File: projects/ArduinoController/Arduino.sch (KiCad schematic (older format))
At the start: 56 parts

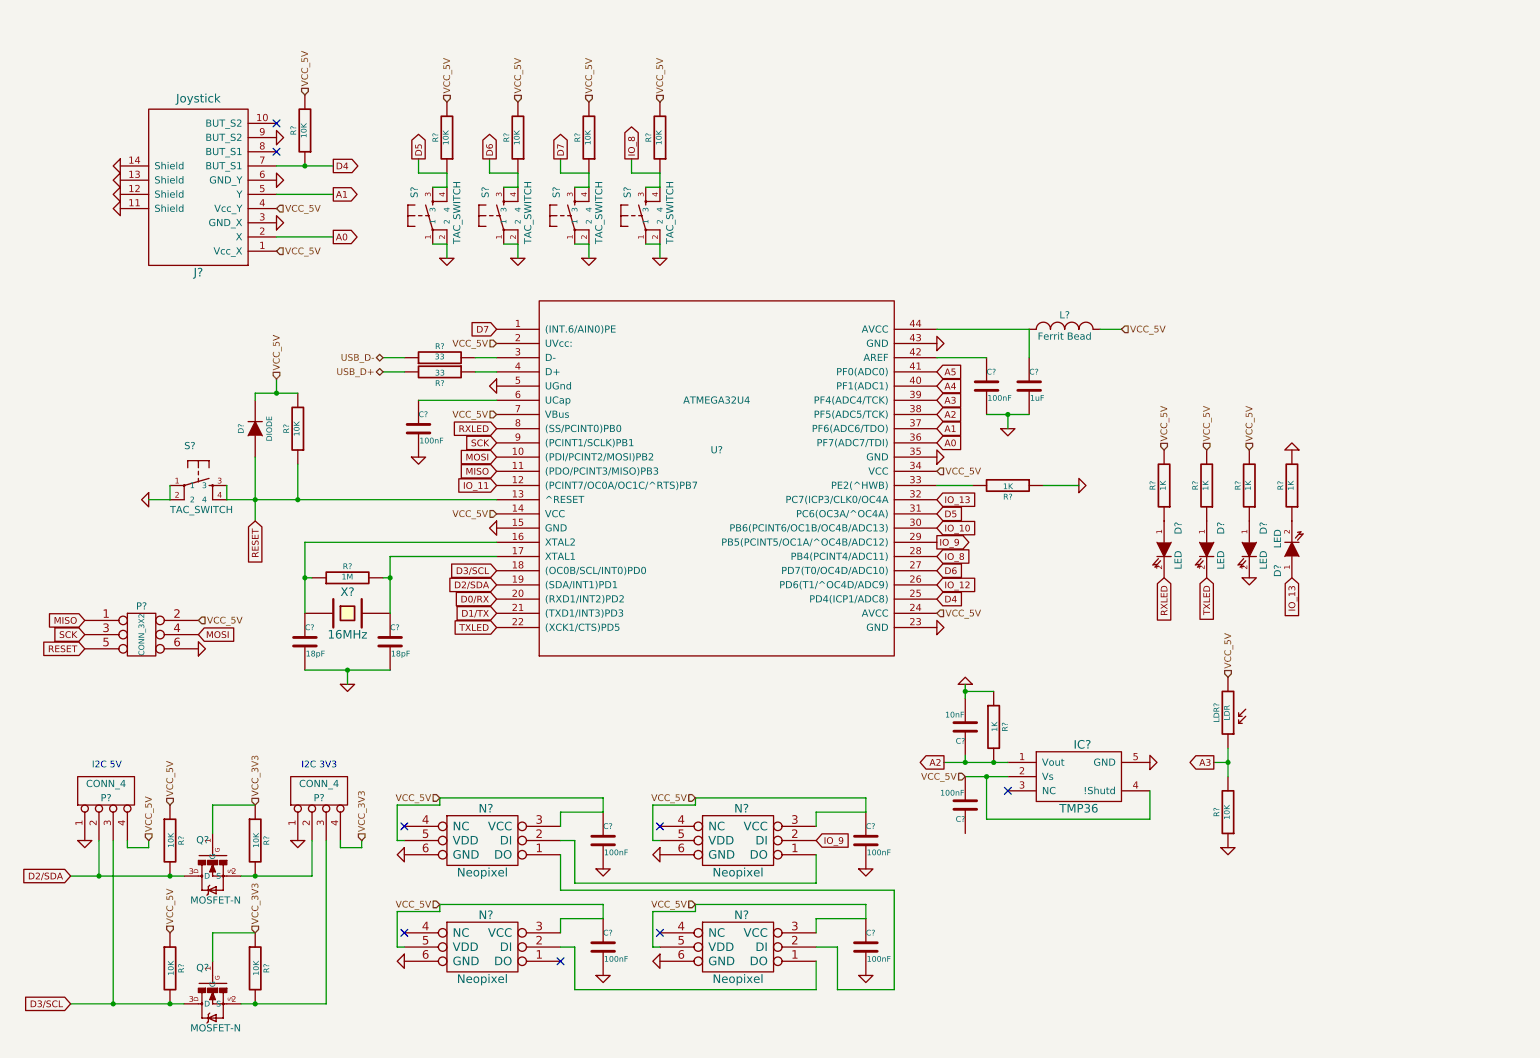
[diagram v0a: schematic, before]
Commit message: working on schematics of Arduino Controller
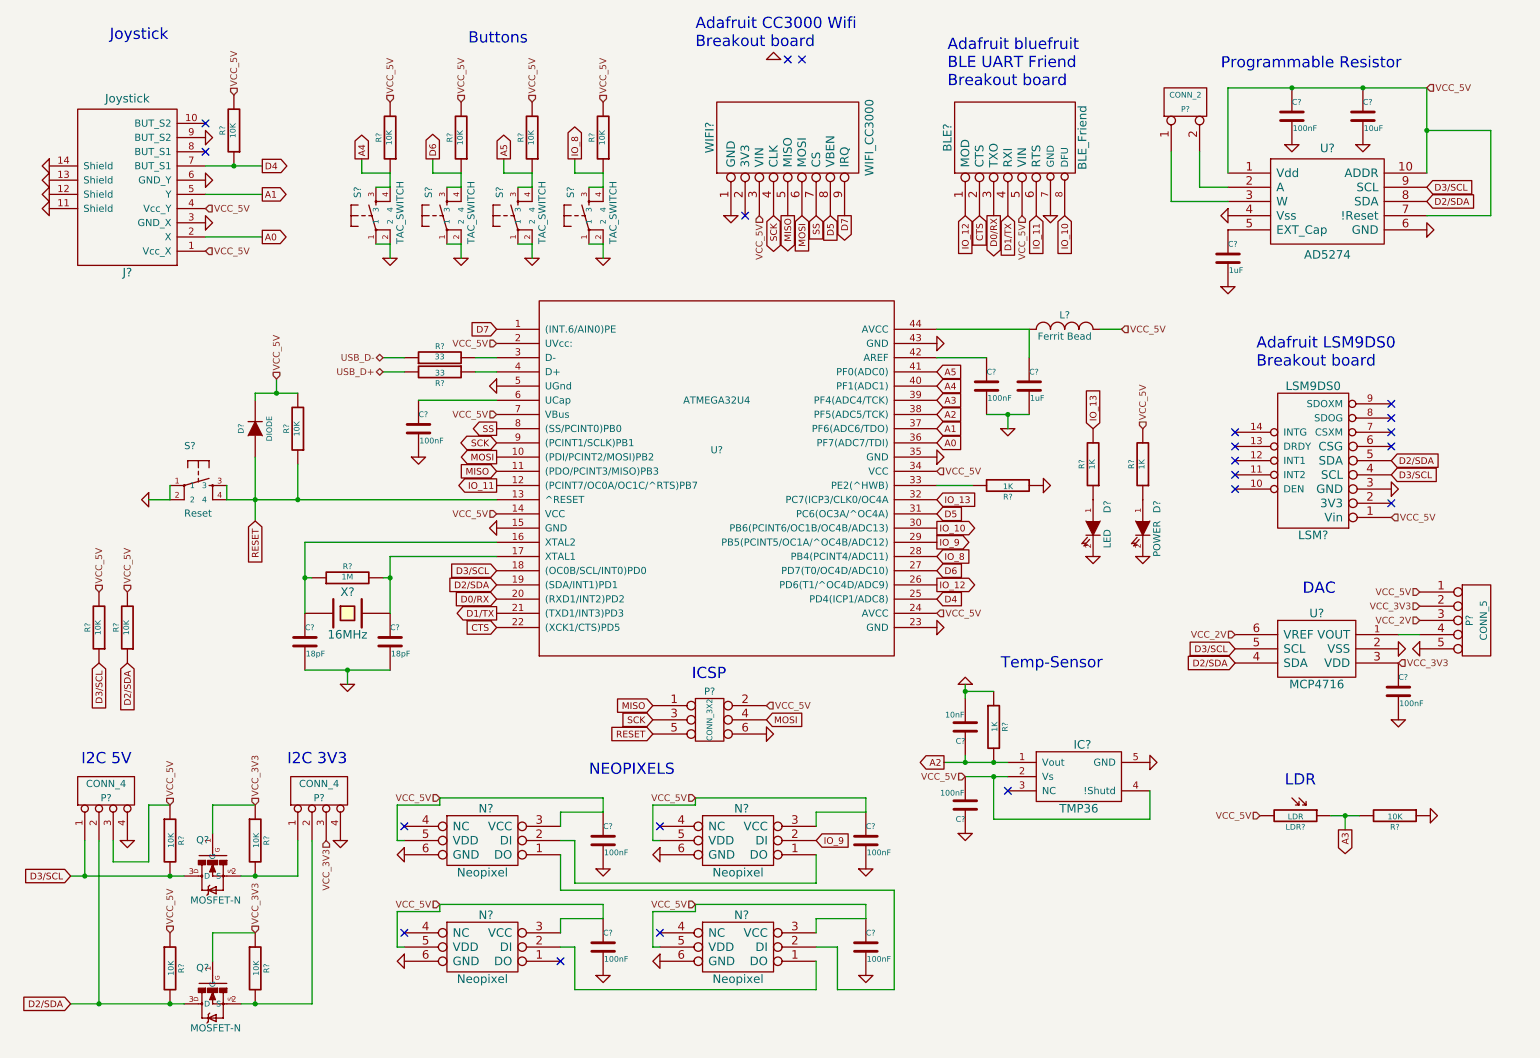
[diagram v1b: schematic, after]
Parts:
- removed D? (x3): LED, symbol LED
- removed R? (x3): 1K, symbol R
- added BLE?: BLE_Friend, symbol BLE_Friend
- added C?: 1uF, symbol C
- added C? (x2): 100nF, symbol C
- added C?: 10uF, symbol C
- added D?: LED, symbol LED
- added LSM?: LSM9DS0, symbol LSM9DS0
- added P?: CONN_2, symbol CONN_2
- added P?: CONN_5, symbol CONN_5
- added R? (x2): 10K, symbol R
- added R?: 1K, symbol R
- added U?: AD5274, symbol AD5274
- added U?: MCP4716, symbol MCP4716
- added WIFI?: WIFI_CC3000, symbol WIFI_CC3000
- D?: value LED -> POWER
- S?: value TAC_SWITCH -> Reset
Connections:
- net A4: now also R?.1, S?.3, S?.4
- net A5: now also R?.1, S?.3, S?.4
- net D0/RX: now also BLE?.3 (TXO)
- net D1/TX: now also BLE?.4 (RXI)
- net D2/SDA: now also Q?.3 (D), R?.2, LSM?.5 (SDA), R?.1, U?.4 (SDA), U?.8 (SDA); no longer Q?.3 (D), R?.2
- net D3/SCL: now also P?.1 (P1), Q?.3 (D), R?.2, LSM?.4 (SCL), R?.1, U?.5 (SCL), U?.9 (SCL); no longer P?.3 (P3), Q?.3 (D), R?.2
- net D5: now also WIFI?.8 (VBEN); no longer R?.1, S?.3, S?.4
- net D7: now also WIFI?.9 (IRQ); no longer R?.1, S?.3, S?.4
- net GND: now also C?.1, P?.4 (P4), P?.4 (P4), BLE?.7 (GND), C?.2, C?.2, C?.2, C?.2, D?.2 (K), LSM?.3 (GND), P?.5, U?.2 (VSS), U?.4 (Vss), U?.6 (GND), WIFI?.1 (GND); no longer P?.1 (P1), P?.1 (P1)
- net IO_10: now also BLE?.8 (DFU)
- net IO_11: now also BLE?.6 (RTS)
- net IO_12: now also BLE?.1 (MOD)
- net IO_13: now also R?.2
- net MISO: now also WIFI?.5 (MISO)
- net MOSI: now also WIFI?.6 (MOSI)
- net SCK: now also WIFI?.4 (CLK)
- net VCC_3V3: now also P?.3 (P3), C?.1, P?.2, U?.3 (VDD); no longer P?.4 (P4)
- net VCC_5V: now also P?.3 (P3), BLE?.5 (VIN), C?.1, C?.1, LSM?.1 (Vin), P?.1, R?.2, R?.2, U?.1 (Vdd), U?.10 (ADDR), U?.7 (!Reset), WIFI?.3 (VIN); no longer P?.4 (P4)
- net at Q?.2 (S), R?.2: now also P?.1 (P1); no longer P?.2 (P2)
- net at Q?.2 (S), R?.2: now also P?.2 (P2); no longer P?.3 (P3)
- net RXLED renamed SS
- net SS: now also WIFI?.7 (CS)
- net TXLED renamed CTS
- net CTS: now also BLE?.2 (CTS)
- new net: C?.1, U?.5 (EXT_Cap)
- new net: P?.2 (PM), U?.2 (A)
- new net: P?.1 (P1), U?.3 (W)
- new net: P?.4, U?.1 (VOUT)
- new net: D?.1 (A), R?.1
- new net VCC_2V: P?.3, U?.6 (VREF)
- no-connect marks 8 -> 21
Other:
- note added: "Adafruit CC3000 Wifi \nBreakout board"
- note added: "Adafruit LSM9DS0\nBreakout board"
- note added: "Adafruit bluefruit \nBLE UART Friend\nBreakout board"
- note added: "Buttons"
- note added: "DAC"
- note added: "ICSP"
- note added: "Joystick"
- note added: "LDR"
- note added: "NEOPIXELS"
- note added: "Programmable Resistor"
- note added: "Temp-Sensor"
- moved on the sheet: D?, J?, LDR?, P?, R?, S?

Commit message: work in progress
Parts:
- added P?: CONN_4, symbol CONN_4
- R? (x2): value 1K -> 220
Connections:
- net D2/SDA: now also P?.2 (P2)
- net D3/SCL: now also P?.1 (P1)
- net GND: now also P?.4 (P4)
- net VCC_5V: now also P?.3 (P3)
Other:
- moved on the sheet: C?, LDR?, N?, P?, R?, WIFI?

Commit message: schematic passes ERC
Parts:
- removed BLE?: BLE_Friend, symbol BLE_Friend
- removed J?: Joystick, symbol Joystick
- removed N? (x4): Neopixel, symbol Neopixel
- removed U?: AD5274, symbol AD5274
- removed WIFI?: WIFI_CC3000, symbol WIFI_CC3000
- added BLE1: BLE_Friend, symbol BLE_Friend
- added C1, C2, C4: 10nF, symbol C
- added J1: Joystick, symbol Joystick
- added N1, N2, N3, N4: Neopixel, symbol Neopixel
- added U3: AD5274, symbol AD5274
- added WIFI1: WIFI_CC3000, symbol WIFI_CC3000
- gave numbers to parts that had none: 58
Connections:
- net A0: now also C1.1, J1.2 (X)
- net A1: now also C2.1, J1.5 (Y)
- net CTS: now also BLE1.2 (CTS)
- net D0/RX: now also BLE1.3 (TXO)
- net D1/TX: now also BLE1.4 (RXI)
- net D2/SDA: now also U3.8 (SDA)
- net D3/SCL: now also U3.9 (SCL)
- net D4: now also C4.1, J1.7 (BUT_S1)
- net D5: now also WIFI1.8 (VBEN)
- net D7: now also WIFI1.9 (IRQ)
- net GND: now also BLE1.7 (GND), C1.2, C2.2, C4.2, J1.3 (GND_X), J1.6 (GND_Y), J1.9 (BUT_S2), N1.6 (GND), N2.6 (GND), N3.6 (GND), N4.6 (GND), U3.4 (Vss), U3.6 (GND), WIFI1.1 (GND)
- net IO_10: now also BLE1.8 (DFU)
- net IO_11: now also BLE1.6 (RTS)
- net IO_12: now also BLE1.1 (MOD)
- net IO_9: now also N3.2 (DI)
- net MISO: now also WIFI1.5 (MISO)
- net MOSI: now also WIFI1.6 (MOSI)
- net SCK: now also WIFI1.4 (CLK)
- net SS: now also WIFI1.7 (CS)
- net VCC_5V: now also BLE1.5 (VIN), J1.1 (Vcc_X), J1.4 (Vcc_Y), N1.3 (VCC), N1.5 (VDD), N2.3 (VCC), N2.5 (VDD), N3.3 (VCC), N3.5 (VDD), N4.3 (VCC), N4.5 (VDD), U3.1 (Vdd), U3.10 (ADDR), U3.7 (!Reset), WIFI1.3 (VIN)
- net at C15.1: now also U3.5 (EXT_Cap)
- net at P5.2 (PM): now also U3.2 (A)
- net at P5.1 (P1): now also U3.3 (W)
- new net: N1.2 (DI), N3.1 (DO)
- new net: N1.1 (DO), N4.2 (DI)
- new net: N2.2 (DI), N4.1 (DO)
- no-connect marks 21 -> 25
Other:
- moved on the sheet: R10, R13, R14, R15, R5, S2, S3, S4, S5

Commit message: working on footprints and netlist
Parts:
- added P5: CONN_1, symbol CONN_1
- renumbered C23 to C16, C24 to C17, C25 to C18, P5 to P6, P6 to P7
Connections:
- no-connect marks 25 -> 24
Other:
- moved on the sheet: BLE1
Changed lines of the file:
@@
 	9850 6150 9850 6050
 Connection ~ 9850 6050
-Text Notes 5300 875  0    79   ~ 0
+Text Notes 5450 1175 0    79   ~ 0
 Adafruit CC3000 Wifi \nBreakout board
 NoConn ~ 5650 2050
@@
 Text GLabel 6250 2050 3    47   Input ~ 0
 D5
-Text GLabel 7200 1900 3    47   Input ~ 0
+Text GLabel 7200 2050 3    47   Input ~ 0
 IO_12
-Text GLabel 7700 1900 3    47   Input ~ 0
+Text GLabel 7700 2050 3    47   Input ~ 0
 IO_11
 Text GLabel 6350 2050 3    47   Output ~ 0
 D7
-Text GLabel 7900 1900 3    47   Input ~ 0
+Text GLabel 7900 2050 3    47   Input ~ 0
 IO_10
 $Comp
@@
 $EndComp
 $Comp
-L C C23
+L C C16
 U 1 1 556B3C92
 P 9500 1200
-F 0 "C23" H 9500 1300 40  0000 L CNN
+F 0 "C16" H 9500 1300 40  0000 L CNN
 F 1 "100nF" H 9506 1115 40  0000 L CNN
 F 2 "" H 9538 1050 30  0000 C CNN
@@
 $EndComp
 $Comp
-L C C24
+L C C17
 U 1 1 556B3C9D
 P 10000 1200
-F 0 "C24" H 10000 1300 40  0000 L CNN
+F 0 "C17" H 10000 1300 40  0000 L CNN
 F 1 "10uF" H 10006 1115 40  0000 L CNN
 F 2 "" H 10038 1050 30  0000 C CNN
@@
 $EndComp
 $Comp
-L CONN_2 P5
+L CONN_2 P6
 U 1 1 556B4F2B
 P 8750 1100
-F 0 "P5" V 8700 1100 40  0000 C CNN
+F 0 "P6" V 8700 1100 40  0000 C CNN
 F 1 "CONN_2" V 8800 1100 40  0000 C CNN
 F 2 "" H 8750 1100 60  0000 C CNN
@@
 $EndComp
 $Comp
-L C C25
+L C C18
 U 1 1 556B8AA1
 P 10250 5250
-F 0 "C25" H 10250 5350 40  0000 L CNN
+F 0 "C18" H 10250 5350 40  0000 L CNN
 F 1 "100nF" H 10256 5165 40  0000 L CNN
 F 2 "" H 10288 5100 30  0000 C CNN
@@
 Text GLabel 3200 1500 1    47   Output ~ 0
 A4
-Text Notes 7075 1025 0    79   ~ 0
+Text Notes 7075 1175 0    79   ~ 0
 Adafruit bluefruit \nBLE UART Friend\nBreakout board
-Text HLabel 7600 1900 3    47   Input ~ 0
+Text HLabel 7600 2050 3    47   Input ~ 0
 VCC_5V
 $Comp
 L GND #PWR042
 U 1 1 556BCBB3
-P 7800 1900
-F 0 "#PWR042" H 7800 1900 30  0001 C CNN
-F 1 "GND" H 7800 1830 30  0001 C CNN
-F 2 "" H 7800 1900 60  0000 C CNN
-F 3 "" H 7800 1900 60  0000 C CNN
-	1    7800 1900
-	1    0    0    -1
-$EndComp
-Text GLabel 7400 1900 3    47   Output ~ 0
+P 7800 2050
+F 0 "#PWR042" H 7800 2050 30  0001 C CNN
+F 1 "GND" H 7800 1980 30  0001 C CNN
+F 2 "" H 7800 2050 60  0000 C CNN
+F 3 "" H 7800 2050 60  0000 C CNN
+	1    7800 2050
+	1    0    0    -1
+$EndComp
+Text GLabel 7400 2050 3    47   Output ~ 0
 D0/RX
-Text GLabel 7500 1900 3    47   Input ~ 0
+Text GLabel 7500 2050 3    47   Input ~ 0
 D1/TX
-NoConn ~ 5950 950
-NoConn ~ 6050 950
-$Comp
-L GND #PWR043
-U 1 1 556BE90D
-P 5850 950
-F 0 "#PWR043" H 5850 950 30  0001 C CNN
-F 1 "GND" H 5850 880 30  0001 C CNN
-F 2 "" H 5850 950 60  0000 C CNN
-F 3 "" H 5850 950 60  0000 C CNN
-	1    5850 950
-	-1   0    0    1
-$EndComp
 Text GLabel 6150 2050 3    47   Input ~ 0
 SS
@@
 Text GLabel 5950 2050 3    47   Output ~ 0
 MISO
-Text GLabel 7300 1900 3    47   Input ~ 0
+Text GLabel 7300 2050 3    47   Input ~ 0
 CTS
 $Comp
@@
 $EndComp
 $Comp
-L GND #PWR044
+L GND #PWR043
 U 1 1 556BF813
 P 8100 4300
-F 0 "#PWR044" H 8100 4300 30  0001 C CNN
+F 0 "#PWR043" H 8100 4300 30  0001 C CNN
 F 1 "GND" H 8100 4230 30  0001 C CNN
 F 2 "" H 8100 4300 60  0000 C CNN
@@
 $EndComp
 $Comp
-L GND #PWR045
+L GND #PWR044
 U 1 1 556BFD01
 P 7200 6250
-F 0 "#PWR045" H 7200 6250 30  0001 C CNN
+F 0 "#PWR044" H 7200 6250 30  0001 C CNN
 F 1 "GND" H 7200 6180 30  0001 C CNN
 F 2 "" H 7200 6250 60  0000 C CNN
@@
 Connection ~ 7400 5850
 $Comp
-L CONN_5 P6
+L CONN_5 P7
 U 1 1 556CA4DE
 P 10800 4750
-F 0 "P6" V 10750 4750 50  0000 C CNN
+F 0 "P7" V 10750 4750 50  0000 C CNN
 F 1 "CONN_5" V 10850 4750 50  0000 C CNN
 F 2 "" H 10800 4750 60  0000 C CNN
@@
 $EndComp
 $Comp
-L GND #PWR046
+L GND #PWR045
 U 1 1 556CA4FA
 P 10400 4950
-F 0 "#PWR046" H 10400 4950 30  0001 C CNN
+F 0 "#PWR045" H 10400 4950 30  0001 C CNN
 F 1 "GND" H 10400 4880 30  0001 C CNN
 F 2 "" H 10400 4950 60  0000 C CNN
@@
 I2C 5V
 $Comp
-L GND #PWR047
+L GND #PWR046
 U 1 1 556E0676
 P 1200 4850
-F 0 "#PWR047" H 1200 4850 30  0001 C CNN
+F 0 "#PWR046" H 1200 4850 30  0001 C CNN
 F 1 "GND" H 1200 4780 30  0001 C CNN
 F 2 "" H 1200 4850 60  0000 C CNN
@@
 Text GLabel 1000 4850 3    47   Input ~ 0
 D2/SDA
-$Comp
-L WIFI_CC3000 WIFI1
-U 1 1 556E9586
-P 5950 1500
-F 0 "WIFI1" H 5950 2050 60  0000 C CNN
-F 1 "WIFI_CC3000" H 5950 925 60  0000 C CNN
-F 2 "" H 5950 1450 60  0000 C CNN
-F 3 "" H 5950 1450 60  0000 C CNN
-	1    5950 1500
-	0    -1   -1   0
-$EndComp
 NoConn ~ 600  1550
 NoConn ~ 600  1650
@@
 Connection ~ 1850 2050
 $Comp
-L GND #PWR048
+L GND #PWR047
 U 1 1 5571681B
 P 2650 1950
-F 0 "#PWR048" H 2650 1950 30  0001 C CNN
+F 0 "#PWR047" H 2650 1950 30  0001 C CNN
 F 1 "GND" H 2650 1880 30  0001 C CNN
 F 2 "" H 2650 1950 60  0000 C CNN
@@
 $EndComp
 $Comp
-L GND #PWR049
+L GND #PWR048
 U 1 1 55716826
 P 2250 2150
-F 0 "#PWR049" H 2250 2150 30  0001 C CNN
+F 0 "#PWR048" H 2250 2150 30  0001 C CNN
 F 1 "GND" H 2250 2080 30  0001 C CNN
 F 2 "" H 2250 2150 60  0000 C CNN
@@
 $EndComp
 $Comp
-L GND #PWR050
+L GND #PWR049
 U 1 1 55716831
 P 1850 2450
-F 0 "#PWR050" H 1850 2450 30  0001 C CNN
+F 0 "#PWR049" H 1850 2450 30  0001 C CNN
 F 1 "GND" H 1850 2380 30  0001 C CNN
 F 2 "" H 1850 2450 60  0000 C CNN
@@
 L BLE_Friend BLE1
 U 1 1 5571909F
-P 7550 1350
-F 0 "BLE1" H 7550 1825 60  0000 C CNN
-F 1 "BLE_Friend" H 7550 875 60  0000 C CNN
-F 2 "" H 7550 1250 60  0000 C CNN
-F 3 "" H 7550 1250 60  0000 C CNN
-	1    7550 1350
+P 7550 1500
+F 0 "BLE1" H 7550 1975 60  0000 C CNN
+F 1 "BLE_Friend" H 7550 1025 60  0000 C CNN
+F 2 "" H 7550 1400 60  0000 C CNN
+F 3 "" H 7550 1400 60  0000 C CNN
+	1    7550 1500
 	0    -1   -1   0
 $EndComp
@@
 $EndComp
 $Comp
-L PWR_FLAG #FLG051
+L PWR_FLAG #FLG050
 U 1 1 55719902
 P 900 3650
-F 0 "#FLG051" H 900 3745 30  0001 C CNN
+F 0 "#FLG050" H 900 3745 30  0001 C CNN
 F 1 "PWR_FLAG" H 900 3830 30  0000 C CNN
 F 2 "" H 900 3650 60  0000 C CNN
@@
 $EndComp
 $Comp
-L GND #PWR052
+L GND #PWR051
 U 1 1 55719914
 P 900 3800
-F 0 "#PWR052" H 900 3800 30  0001 C CNN
+F 0 "#PWR051" H 900 3800 30  0001 C CNN
 F 1 "GND" H 900 3730 30  0001 C CNN
 F 2 "" H 900 3800 60  0000 C CNN
@@
 	-1   0    0    1
 $EndComp
+$Comp
+L CONN_1 P5
+U 1 1 5575D7F0
+P 6800 1775
+F 0 "P5" H 6880 1775 40  0000 L CNN
+F 1 "CONN_1" H 6800 1830 30  0001 C CNN
+F 2 "" H 6800 1775 60  0000 C CNN
+F 3 "" H 6800 1775 60  0000 C CNN
+	1    6800 1775
+	0    -1   -1   0
+$EndComp
+NoConn ~ 6800 1925
+$Comp
+L WIFI_CC3000 WIFI1
+U 1 1 5575FBE6
+P 5950 1500
+F 0 "WIFI1" H 5950 2050 60  0000 C CNN
+F 1 "WIFI_CC3000" H 5950 925 60  0000 C CNN
+F 2 "" H 5950 1450 60  0000 C CNN
+F 3 "" H 5950 1450 60  0000 C CNN
+	1    5950 1500
+	0    -1   -1   0
+$EndComp
 $EndSCHEMATC

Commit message: footprints done
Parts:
- added C10, C13, C14, C9: 100nF, symbol C
- added D5: TX, symbol LED
- added D6: RX, symbol LED
- added N3, N4, N7, N8: Neopixel, symbol Neopixel
- added P4, P5: CONN_4, symbol CONN_4
- added R22, R23: 220, symbol R
- added U3: PCF8574, symbol PCF8574
- renumbered C9 to C11, C10 to C12, C11 to C15, C12 to C16, C13 to C17, C14 to C18, C15 to C26, C16 to C27, C17 to C28, C18 to C29, N3 to N5, N4 to N6, P4 to P6, P5 to P7, P6 to P8, P7 to P9, R4 to R1, R20 to R19, R3 to R2, R19 to R20, R1 to R3, R2 to R4, U3 to U2, U2 to U7
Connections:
- net A4: now also P4.1 (P1); no longer R10.1, S2.3, S2.4
- net A5: now also P4.2 (P2); no longer R14.1, S4.3, S4.4
- net D2/SDA: now also U3.15 (SDA)
- net D3/SCL: now also U3.14 (SCL)
- net D4: now also WIFI1.7 (CS); no longer C4.1, J1.7 (BUT_S1), R5.1
- net D6: now also P5.1 (P1); no longer R13.1, S3.3, S3.4
- net GND: now also BLE1.2 (CTS), C10.2, C13.2, C14.2, C9.2, N3.6 (GND), N4.6 (GND), N7.6 (GND), N8.6 (GND), P4.4 (P4), P5.4 (P4), U3.1 (A0), U3.2 (A1), U3.3 (A3), U3.8 (VSS)
- net IO_8: now also P5.2 (P2); no longer R15.1, S5.3, S5.4
- net VCC_5V: now also C10.1, C13.1, C14.1, C9.1, N3.3 (VCC), N3.5 (VDD), N4.3 (VCC), N4.5 (VDD), N7.3 (VCC), N7.5 (VDD), N8.3 (VCC), N8.5 (VDD), P4.3 (P3), P5.3 (P3), R22.2, R23.2, U3.16 (VDD)
- net at N2.1 (DO): now also N7.2 (DI)
- net CTS renamed TXLED
- net TXLED: now also D5.2 (K); no longer BLE1.2 (CTS)
- net SS renamed RXLED
- net RXLED: now also D6.2 (K); no longer WIFI1.7 (CS)
- new net: D5.1 (A), R22.1
- new net: D6.1 (A), R23.1
- new net: N3.2 (DI), N7.1 (DO)
- new net: N3.1 (DO), N8.2 (DI)
- new net: N4.2 (DI), N8.1 (DO)
- new net P0: R10.1, S2.3, S2.4, U3.4 (P0)
- new net P1: R13.1, S3.3, S3.4, U3.5 (P1)
- new net P2: R14.1, S4.3, S4.4, U3.6 (P2)
- new net P3: R15.1, S5.3, S5.4, U3.7 (P3)
- new net P4: C4.1, J1.7 (BUT_S1), R5.1, U3.9 (P4)
- no-connect marks 24 -> 32
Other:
- note added: "ANALOG"
- note added: "DIGITAL"
- note added: "GROVE"
- moved on the sheet: BLE1, C1, C11, C12, C17, C18, C2, C26, C27, C28, C29, C3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
